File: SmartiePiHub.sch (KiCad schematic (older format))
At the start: 57 parts, among them P1 Conn_02x20_Odd_Even

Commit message: finishing power supply. adding trx pmod.
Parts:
- removed CN?: ZWAVE_TRX_HEADER, symbol Connector_Generic:Conn_02x04_Odd_Even
- added C?: 4.7uF, symbol Device:C_Small
- added CN?: ZWAVE_TRX_HEADER, symbol Connector_Generic:Conn_02x06_Top_Bottom
- added CN?: ZIGBEE_TRX_HEADER, symbol Connector_Generic:Conn_02x06_Top_Bottom
- added D? (x2): D_Schottky, symbol Device:D_Schottky
- added J?: USB_B_Micro, symbol Connector:USB_B_Micro
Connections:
- net +3V3: now also CN?.12 (Pin_12), CN?.12 (Pin_12), CN?.6 (Pin_6), CN?.6 (Pin_6)
- net +5V: now also D?.1 (K), D?.1 (K); no longer C?.1, C?.1, D?.1 (K), U?.4 (VOUT)
- net +5VUSB: now also C?.1, D?.2 (A), J?.1 (VBUS)
- net GND: now also C?.2, CN?.11 (Pin_11), CN?.11 (Pin_11), CN?.5 (Pin_5), CN?.5 (Pin_5), J?.5 (GND)
- net SPI1_MISO: now also CN?.3 (Pin_3), CN?.3 (Pin_3)
- net SPI1_MOSI: now also CN?.2 (Pin_2), CN?.2 (Pin_2)
- net SPI1_SCK: now also CN?.4 (Pin_4), CN?.4 (Pin_4)
- new net: C?.1, C?.1, D?.1 (K), D?.2 (A), U?.4 (VOUT)
- new net ZIGBEE_INT: CN?.7 (Pin_7)
- new net ZIGBEE_WAKE: CN?.9 (Pin_9)
- new net ZWAVE_CS: CN?.1 (Pin_1), CN?.1 (Pin_1)
- new net ZWAVE_INT: CN?.7 (Pin_7)
- new net ZWAVE_WAKE: CN?.9 (Pin_9)
- new net ~ZIGBEE_RST: CN?.8 (Pin_8)
- new net ~ZWAVE_RST: CN?.8 (Pin_8)
- no-connect marks 7 -> 13

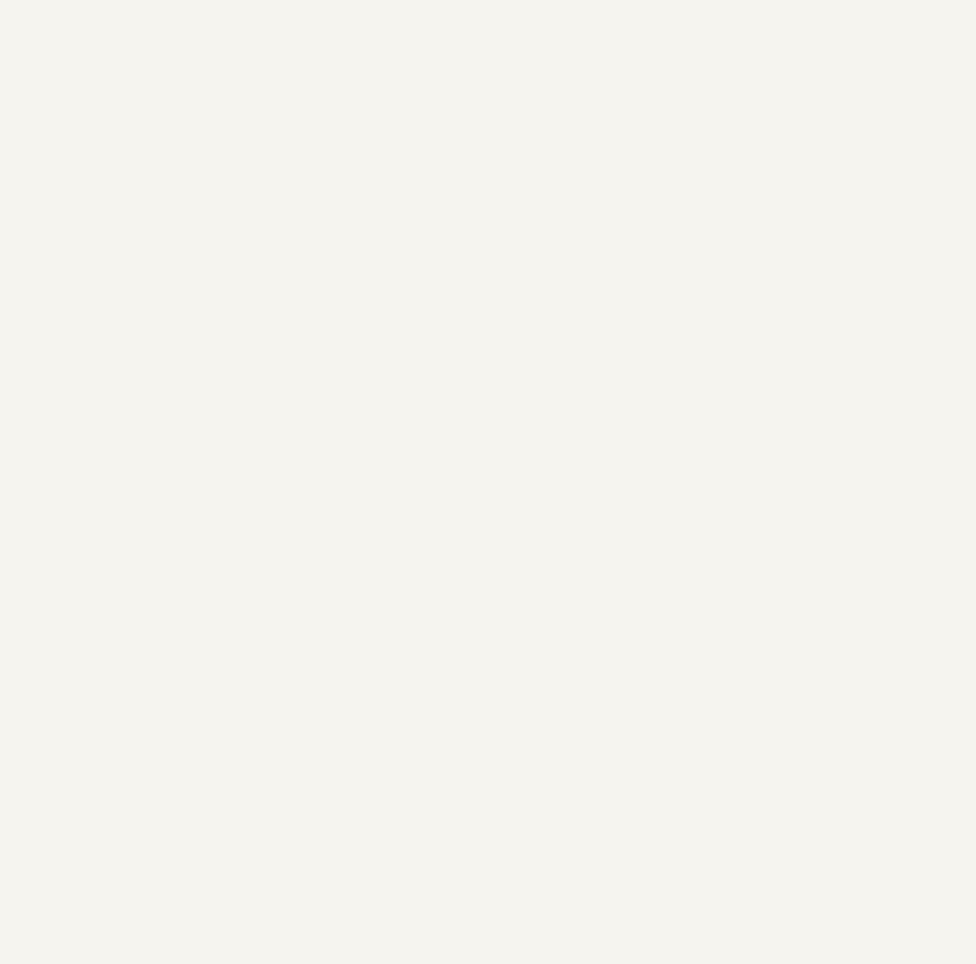
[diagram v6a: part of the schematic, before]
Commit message: added microphones
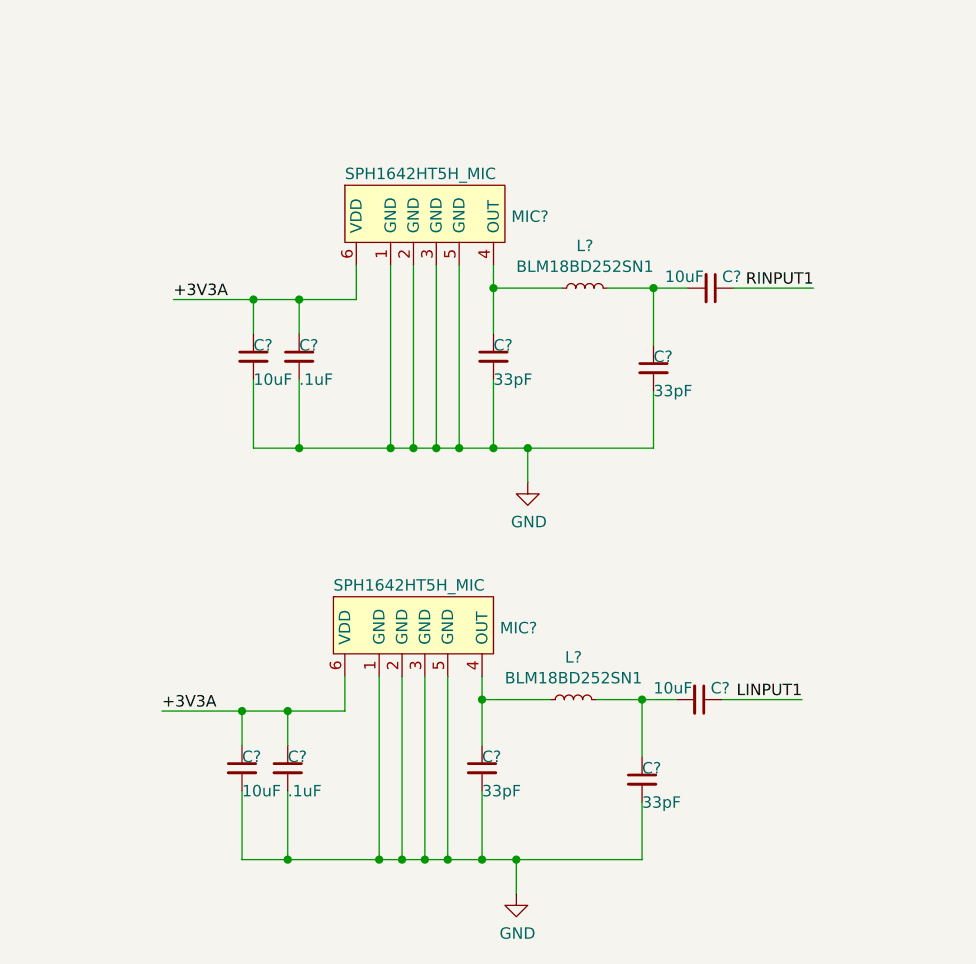
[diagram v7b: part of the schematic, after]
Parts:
- added C? (x4): 10uF, symbol Device:C_Small
- added C? (x2): .1uF, symbol Device:C_Small
- added C? (x4): 33pF, symbol Device:C_Small
- added L? (x2): BLM18BD252SN1, symbol Device:L_Small
- added MIC? (x2): SPH1642HT5H_MIC, symbol smartie-pi-hub:SPH1642HT5H_MIC
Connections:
- net +3V3A: now also C?.1, C?.1, C?.1, C?.1, MIC?.6 (VDD), MIC?.6 (VDD)
- net GND: now also C?.2, C?.2, C?.2, C?.2, C?.2, C?.2, C?.2, C?.2, MIC?.1 (GND), MIC?.1 (GND), MIC?.2 (GND), MIC?.2 (GND), MIC?.3 (GND), MIC?.3 (GND), MIC?.5 (GND), MIC?.5 (GND)
- net LINPUT1: now also C?.1
- net RINPUT1: now also C?.1
- new net: C?.1, L?.1, MIC?.4 (OUT) (x2)
- new net: C?.1, C?.2, L?.2 (x2)

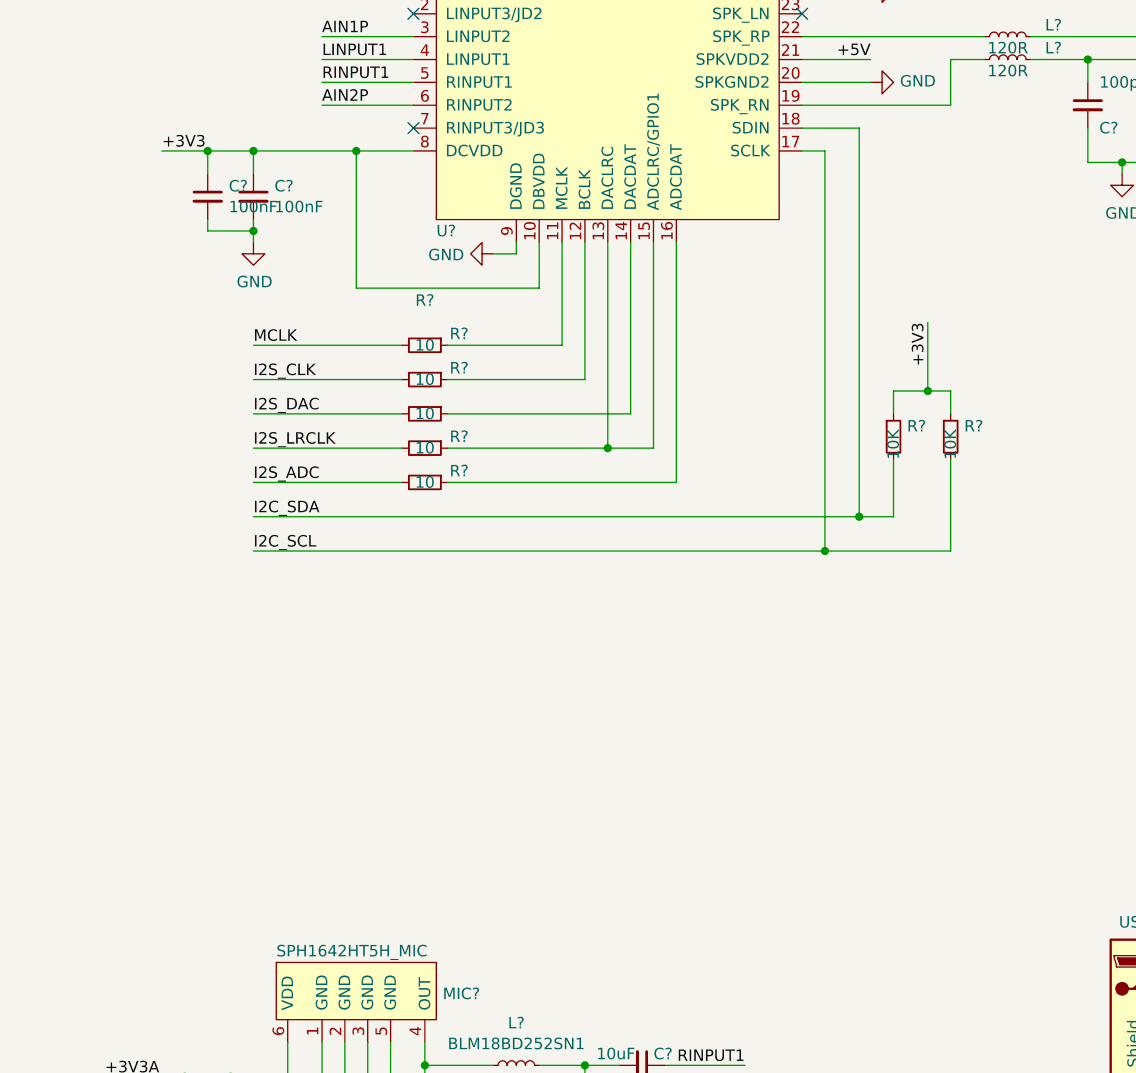
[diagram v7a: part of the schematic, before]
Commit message: adding oscillator
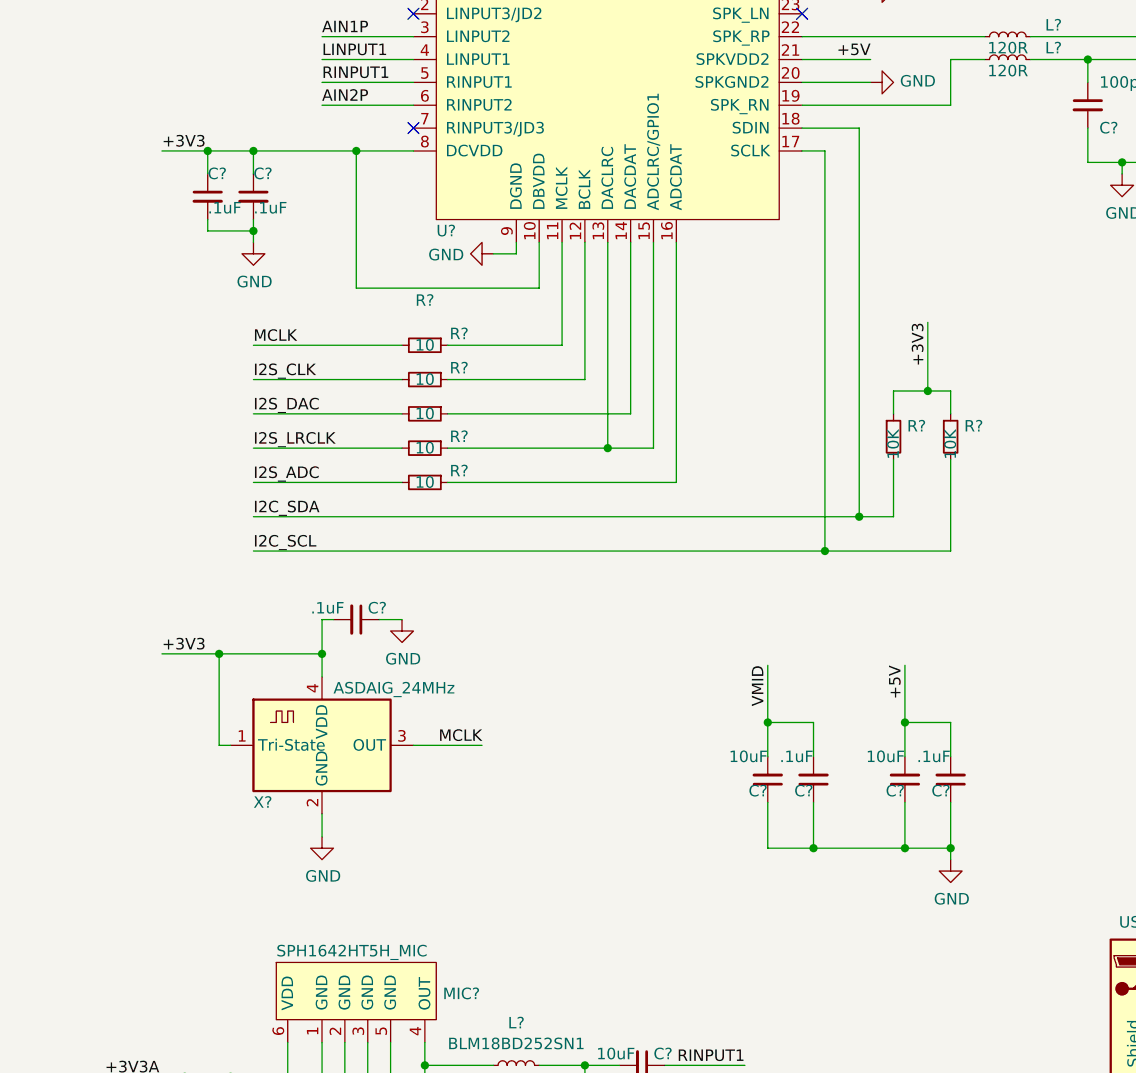
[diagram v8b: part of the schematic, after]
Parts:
- added C? (x2): 10uF, symbol Device:C_Small
- added C? (x3): .1uF, symbol Device:C_Small
- added X?: ASDAIG_24MHz, Oscillator:Oscillator_SMD_Abracon_ASCO-4Pin_1.6x1.2mm, symbol Oscillator:ASCO
- C? (x2): value 100nF -> .1uF
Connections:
- net +3V3: now also C?.2, X?.1 (Tri-State), X?.4 (VDD)
- net +5V: now also C?.2, C?.2
- net GND: now also C?.1, C?.1, C?.1, C?.1, C?.1, X?.2 (GND)
- net MCLK: now also X?.3 (OUT)
- net VMID: now also C?.2, C?.2
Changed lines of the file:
@@
 U 1 1 5EC04346
 P 6600 3150
-F 0 "C?" H 6692 3196 50  0000 L CNN
-F 1 "100nF" H 6692 3105 50  0000 L CNN
+F 0 "C?" H 6600 3250 50  0000 L CNN
+F 1 ".1uF" H 6600 3100 50  0000 L CNN
 F 2 "" H 6600 3150 50  0001 C CNN
 F 3 "~" H 6600 3150 50  0001 C CNN
@@
 U 1 1 5EC04C5E
 P 6400 3150
-F 0 "C?" H 6492 3196 50  0000 L CNN
-F 1 "100nF" H 6492 3105 50  0000 L CNN
+F 0 "C?" H 6400 3250 50  0000 L CNN
+F 1 ".1uF" H 6400 3100 50  0000 L CNN
 F 2 "" H 6400 3150 50  0001 C CNN
 F 3 "~" H 6400 3150 50  0001 C CNN
@@
 Text Label 8750 6950 2    50   ~ 0
 RINPUT1
+$Comp
+L Device:C_Small C?
+U 1 1 5EC0E6FA
+P 8850 5700
+F 0 "C?" H 8850 5750 50  0000 L CNN
+F 1 "10uF" H 8850 5600 50  0000 L CNN
+F 2 "" H 8850 5700 50  0001 C CNN
+F 3 "~" H 8850 5700 50  0001 C CNN
+	1    8850 5700
+	-1   0    0    1
+$EndComp
+$Comp
+L Device:C_Small C?
+U 1 1 5EC0F27C
+P 9050 5700
+F 0 "C?" H 9050 5750 50  0000 L CNN
+F 1 ".1uF" H 9050 5600 50  0000 L CNN
+F 2 "" H 9050 5700 50  0001 C CNN
+F 3 "~" H 9050 5700 50  0001 C CNN
+	1    9050 5700
+	-1   0    0    1
+$EndComp
+$Comp
+L Device:C_Small C?
+U 1 1 5EC0FDFE
+P 9450 5700
+F 0 "C?" H 9450 5750 50  0000 L CNN
+F 1 "10uF" H 9450 5600 50  0000 L CNN
+F 2 "" H 9450 5700 50  0001 C CNN
+F 3 "~" H 9450 5700 50  0001 C CNN
+	1    9450 5700
+	-1   0    0    1
+$EndComp
+$Comp
+L Device:C_Small C?
+U 1 1 5EC0FE04
+P 9650 5700
+F 0 "C?" H 9650 5750 50  0000 L CNN
+F 1 ".1uF" H 9650 5600 50  0000 L CNN
+F 2 "" H 9650 5700 50  0001 C CNN
+F 3 "~" H 9650 5700 50  0001 C CNN
+	1    9650 5700
+	-1   0    0    1
+$EndComp
+Wire Wire Line
+	8850 5800 8850 6000
+Wire Wire Line
+	8850 6000 9050 6000
+Wire Wire Line
+	9650 6000 9650 5800
+Wire Wire Line
+	9450 5800 9450 6000
+Connection ~ 9450 6000
+Wire Wire Line
+	9450 6000 9650 6000
+Wire Wire Line
+	9050 5800 9050 6000
+Connection ~ 9050 6000
+Wire Wire Line
+	9050 6000 9450 6000
+Wire Wire Line
+	9650 6000 9650 6050
+Connection ~ 9650 6000
+$Comp
+L power:GND #PWR?
+U 1 1 5ECCB691
+P 9650 6050
+F 0 "#PWR?" H 9650 5800 50  0001 C CNN
+F 1 "GND" H 9655 5877 50  0000 C CNN
+F 2 "" H 9650 6050 50  0001 C CNN
+F 3 "" H 9650 6050 50  0001 C CNN
+	1    9650 6050
+	1    0    0    -1
+$EndComp
+Wire Wire Line
+	9650 5600 9650 5450
+Wire Wire Line
+	9650 5450 9450 5450
+Wire Wire Line
+	9450 5450 9450 5600
+Wire Wire Line
+	9450 5450 9450 5200
+Connection ~ 9450 5450
+Wire Wire Line
+	9050 5600 9050 5450
+Wire Wire Line
+	9050 5450 8850 5450
+Wire Wire Line
+	8850 5450 8850 5600
+Wire Wire Line
+	8850 5450 8850 5200
+Connection ~ 8850 5450
+Text Label 8850 5200 3    50   ~ 0
+VMID
+Text Label 9450 5200 3    50   ~ 0
++5V
+$Comp
+L Oscillator:ASCO X?
+U 1 1 5ED926D9
+P 6900 5550
+F 0 "X?" H 6600 5300 50  0000 L CNN
+F 1 "ASDAIG_24MHz" H 6950 5800 50  0000 L CNN
+F 2 "Oscillator:Oscillator_SMD_Abracon_ASCO-4Pin_1.6x1.2mm" H 7000 5200 50  0001 C CNN
+F 3 "https://abracon.com/Oscillators/ASCO.pdf" H 6675 5675 50  0001 C CNN
+	1    6900 5550
+	1    0    0    -1
+$EndComp
+Wire Wire Line
+	6900 5250 6900 5150
+Wire Wire Line
+	6900 5150 6450 5150
+Wire Wire Line
+	6450 5150 6450 5550
+Wire Wire Line
+	6450 5550 6500 5550
+Wire Wire Line
+	6450 5150 6200 5150
+Connection ~ 6450 5150
+Text Label 6200 5150 0    50   ~ 0
++3V3
+Wire Wire Line
+	7300 5550 7600 5550
+Text Label 7600 5550 2    50   ~ 0
+MCLK
+Wire Wire Line
+	6900 5850 6900 5950
+$Comp
+L power:GND #PWR?
+U 1 1 5EE3A198
+P 6900 5950
+F 0 "#PWR?" H 6900 5700 50  0001 C CNN
+F 1 "GND" H 6905 5777 50  0000 C CNN
+F 2 "" H 6900 5950 50  0001 C CNN
+F 3 "" H 6900 5950 50  0001 C CNN
+	1    6900 5950
+	1    0    0    -1
+$EndComp
+$Comp
+L Device:C_Small C?
+U 1 1 5EE3AAB2
+P 7050 5000
+F 0 "C?" V 7000 5050 50  0000 L CNN
+F 1 ".1uF" V 7000 4800 50  0000 L CNN
+F 2 "" H 7050 5000 50  0001 C CNN
+F 3 "~" H 7050 5000 50  0001 C CNN
+	1    7050 5000
+	0    1    1    0
+$EndComp
+Wire Wire Line
+	6950 5000 6900 5000
+Wire Wire Line
+	6900 5000 6900 5150
+Connection ~ 6900 5150
+Wire Wire Line
+	7150 5000 7250 5000
+$Comp
+L power:GND #PWR?
+U 1 1 5EE91028
+P 7250 5000
+F 0 "#PWR?" H 7250 4750 50  0001 C CNN
+F 1 "GND" H 7255 4827 50  0000 C CNN
+F 2 "" H 7250 5000 50  0001 C CNN
+F 3 "" H 7250 5000 50  0001 C CNN
+	1    7250 5000
+	1    0    0    -1
+$EndComp
 $EndSCHEMATC
